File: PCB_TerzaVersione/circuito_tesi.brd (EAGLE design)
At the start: 100 x 80 mm, 57 parts, among them IC1 SCD41-D-R2, J2 S5B-ZR-SM4A-TF_(LF)_(SN)CONN_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, Q1 BSS138, Q2 BSS138, Q3 BSS138, Q4 BSS138, U1 STMICROELECTRONICS_LIS3DHSTMI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, U3 MICS-6814, U6 BME280, Y1 ECS-.327-9-16-TR

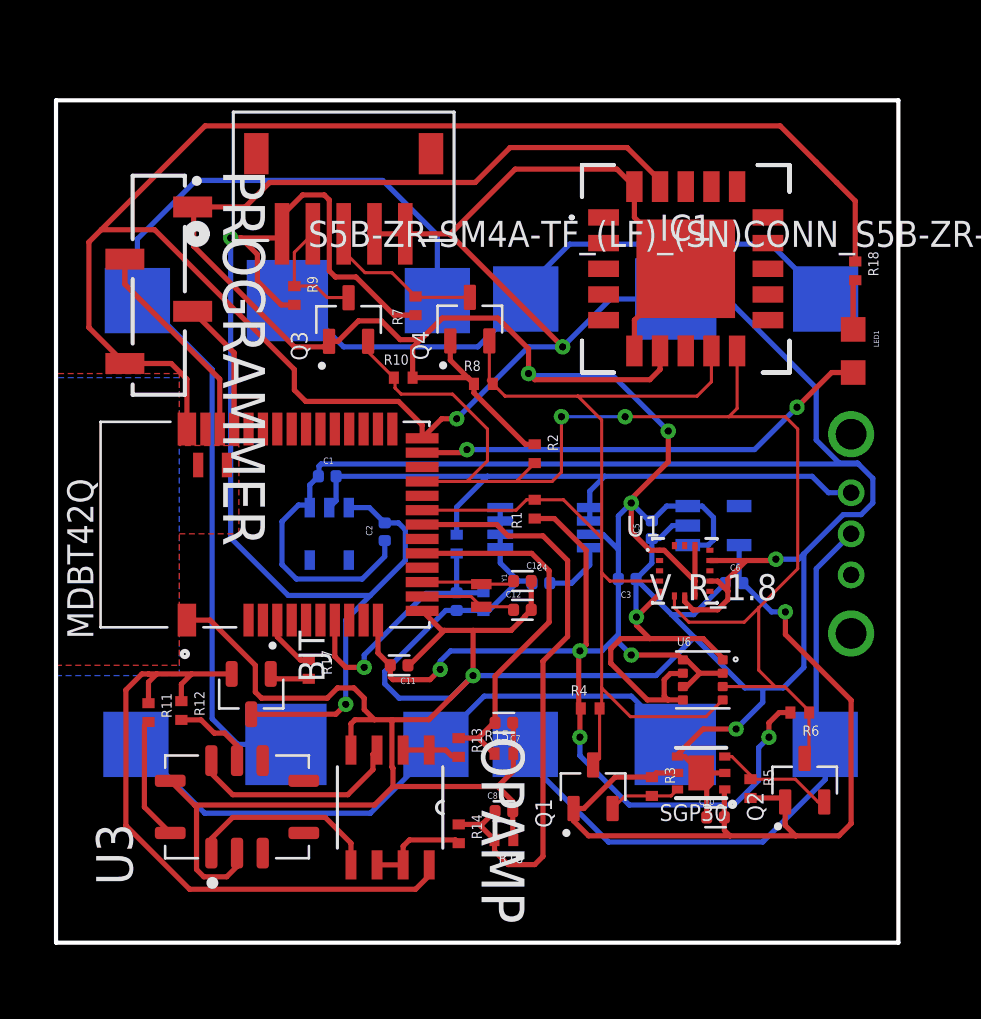
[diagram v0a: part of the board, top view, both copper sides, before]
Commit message: Cambiato collegamento BJT
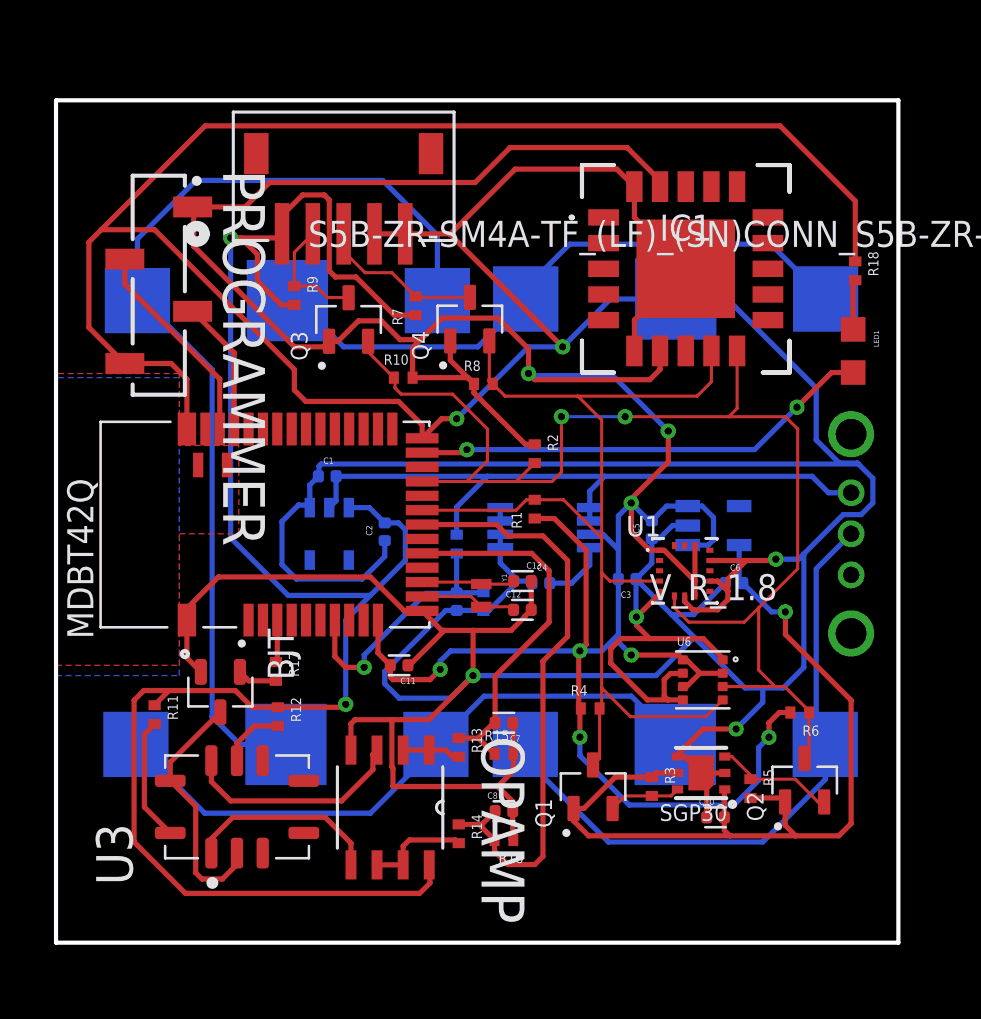
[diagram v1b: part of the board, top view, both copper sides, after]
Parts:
- moved R12 4.71 mm to (20.8, 38.0)
- moved R17 1.60 mm to (20.7, 40.2)
- moved BJT 1.50 mm to (18.0, 39.2)
- moved R11 0.32 mm to (14.8, 38.1)
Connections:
- net 5V: now also OPAMP.8, R11.1, R12.1; no longer BJT.3
- net BJT: now also BJT.3, U3.B, U3.J; no longer BJT.2, OPAMP.8, R11.1, R12.1
- net GND: now also BJT.2; no longer U3.B, U3.J
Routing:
- net 5V: track 59.8 -> 90.3 mm
- net BJT: track 32.0 -> 12.3 mm
- net GND: track 344.6 -> 330.3 mm
- net N$11: track 3.96 -> 3.19 mm
- net P8: track 2.81 -> 2.07 mm

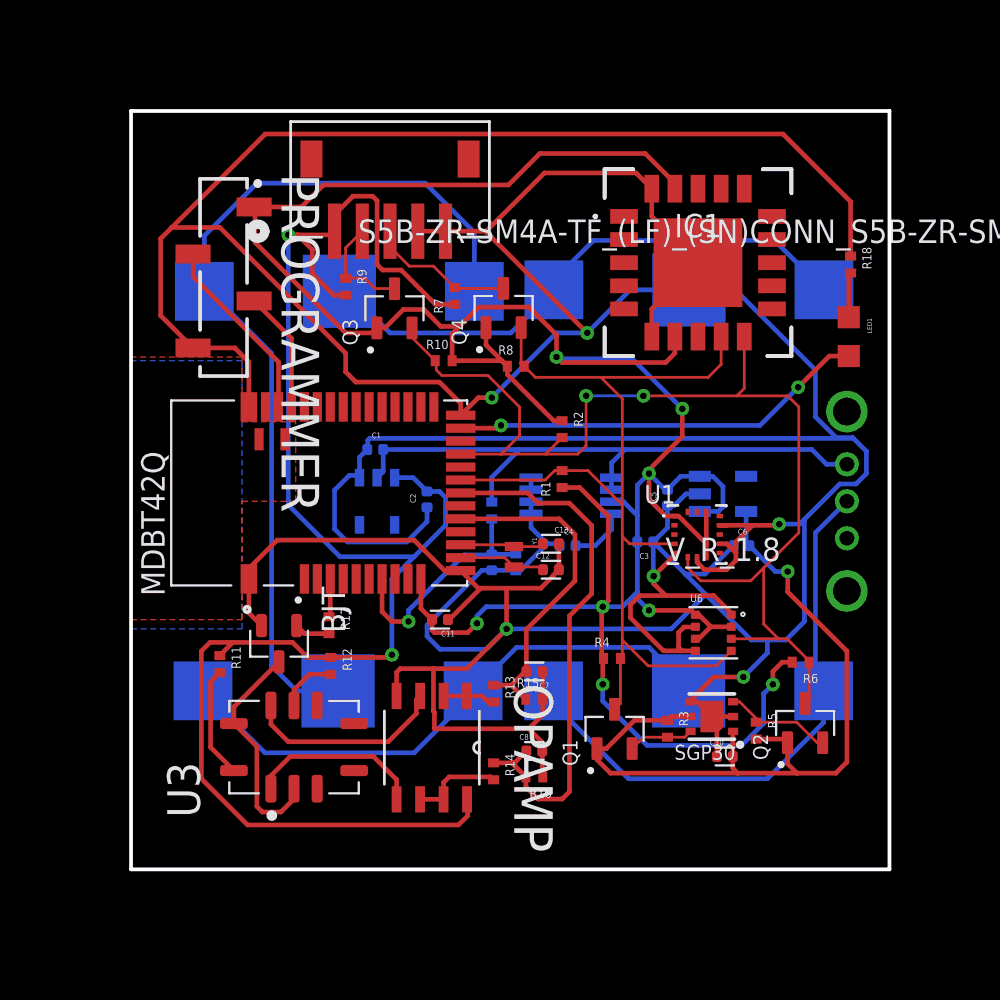
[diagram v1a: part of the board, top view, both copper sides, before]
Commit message: Resistenze con valore esatto
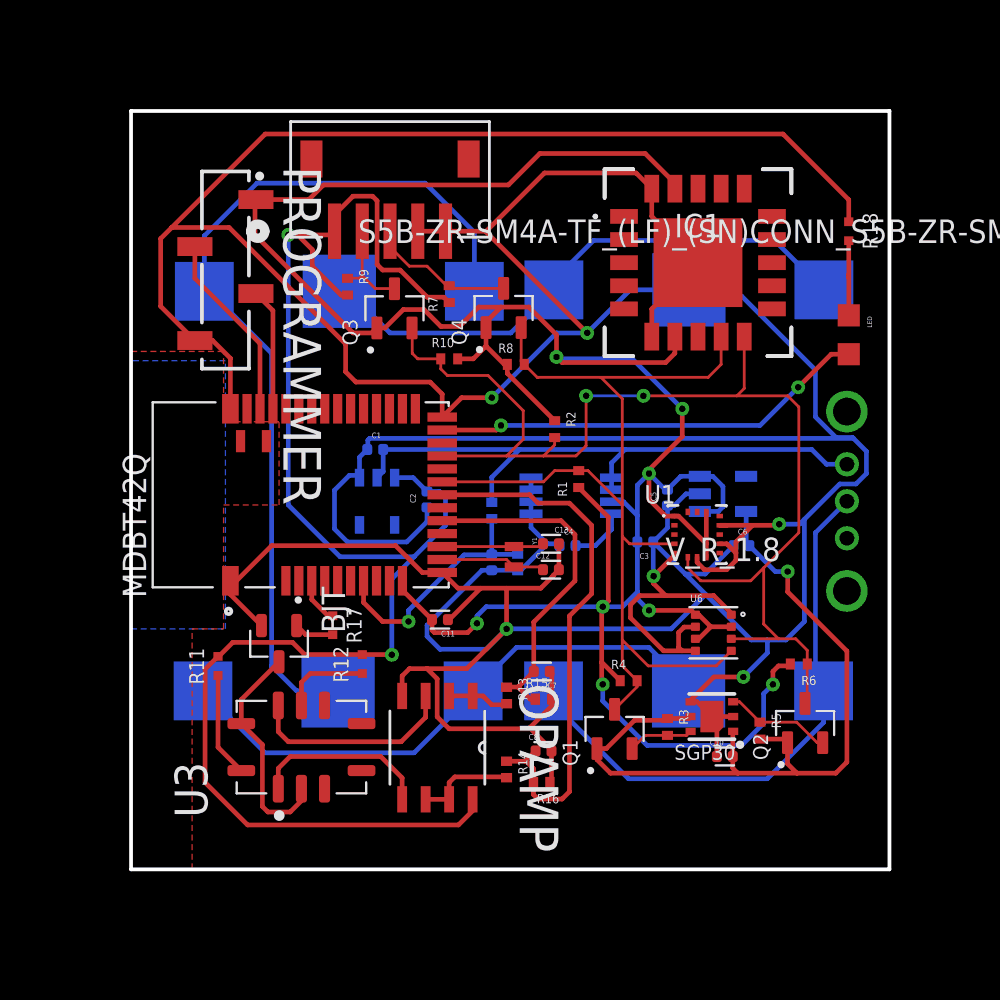
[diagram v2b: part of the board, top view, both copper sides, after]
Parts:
- removed LED1: LTST-C170TBKT, LED_0805:DIOC200X125X110
- added LED: LTST-C170KRKT, LED_R_LTST-C170KRKT:DIOC200X125X110
- R1, R10, R2, R3, R4, R5, R6, R7, R8, R9: value 8-1879333-9 -> MCS0402MC1002FE000; device Resistenza_case_0402:RESC1005X35N -> Res_10K_0402:RESC1005X37N
- R11: value 8-1879333-9 -> ERJPA2F1300X; device Resistenza_case_0402:RESC1005X35N -> Res_130_0402:RES_ERJPA2F1300X
- R12: value 8-1879333-9 -> ERJPA2J821X; device Resistenza_case_0402:RESC1005X35N -> Res_820_0402:RES_ERJPA2J821X
- R13, R14, R19, R20: value 8-1879333-9 -> ERJ-2GEJ515X; device Resistenza_case_0402:RESC1005X35N -> Res_5,1M_0402:RESC1005X40N
- R15, R16: value 8-1879333-9 -> ERJ-2GEJ106X; device Resistenza_case_0402:RESC1005X35N -> Res_10M_0402:RESC1005X40N
- R17: value 8-1879333-9 -> ERJPA2F5101X; device Resistenza_case_0402:RESC1005X35N -> Res_5,1K_0402:RES_ERJPA2F5101X
- R18: value 8-1879333-9 -> ERA2AEB331X; device Resistenza_case_0402:RESC1005X35N -> Res_330_0402:RES_ERA2AEB331X
- moved R18 1.80 mm to (48.8, 61.5)
- moved R12 1.70 mm to (22.5, 38.1), turned to 90 degrees
- moved R4 1.50 mm to (36.9, 37.2)
- moved MDBT42Q 1.00 mm to (19.2, 47.2)
- moved R1 0.90 mm to (34.2, 48.1)
- moved R13 0.71 mm to (30.3, 36.4)
- moved R14 0.71 mm to (30.3, 32.4)
- moved R16 0.50 mm to (32.2, 31.7)
- moved C8 0.50 mm to (32.3, 33.4)
- moved R15 0.50 mm to (32.3, 36.2)
- moved PROGRAMMER 0.41 mm to (15.1, 59.4)
- moved C7 0.40 mm to (32.2, 37.7)
- moved U3 0.40 mm to (19.2, 33.6)
- moved R2 0.40 mm to (32.9, 50.8)
- moved R10 0.32 mm to (27.2, 54.6)
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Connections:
- net 5V: now also R11.2, R12.2; no longer R11.1, R12.1
- net LED: now also LED.+; no longer LED1.+
- net N$11: now also R12.1; no longer R12.2
- net N$13: now also R11.1; no longer R11.2
- net N$9: now also LED.-; no longer LED1.-
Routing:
- net SDA: track 63.2 -> 65.6 mm
- net 5V: track 90.3 -> 88.0 mm
- net GND: track 330.3 -> 328.6 mm
- net SCL: track 53.1 -> 54.7 mm
- net 3.3V: track 154.3 -> 152.7 mm
- net N$9: track 2.43 -> 4.04 mm
- net N$11: track 3.19 -> 4.74 mm
- net LED: track 22.6 -> 23.7 mm
- net N$18: track 4.55 -> 5.51 mm
- net N$17: track 4.72 -> 5.68 mm
- net BATTERY: track 13.0 -> 13.7 mm
- net AIN1: track 18.2 -> 18.8 mm
- net N$13: track 6.17 -> 5.67 mm

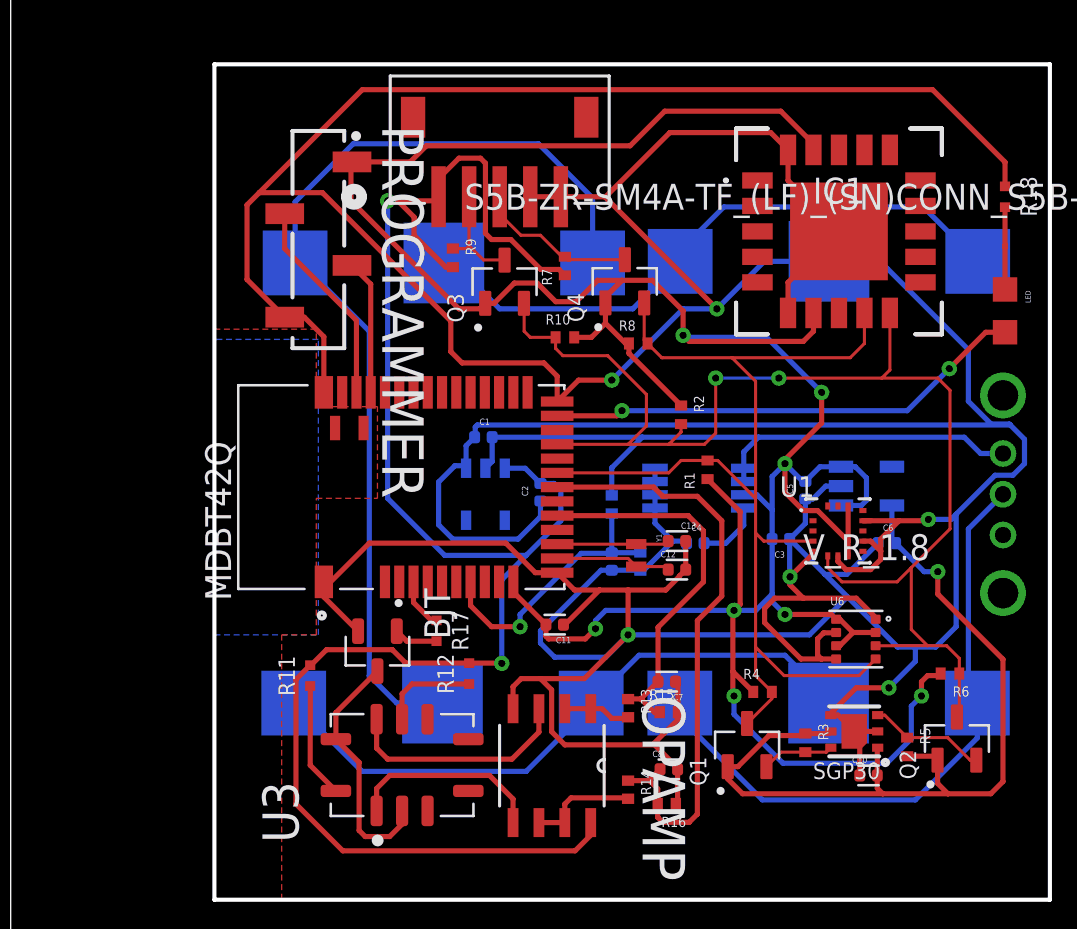
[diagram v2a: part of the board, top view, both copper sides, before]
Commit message: Messi condensatori corretti
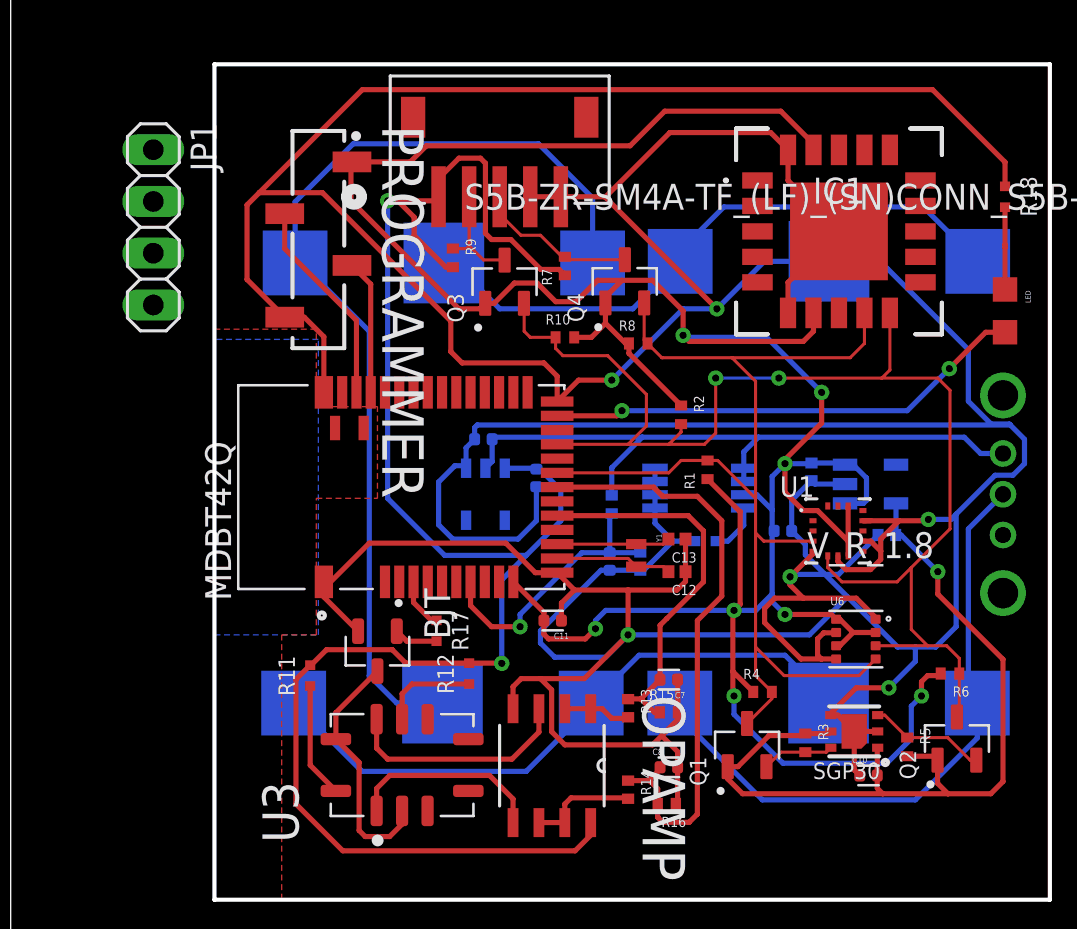
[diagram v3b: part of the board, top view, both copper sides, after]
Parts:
- added JP1: (no value), pinhead:1X04
- C1, C10, C2: value C0402H102J5GACTU -> C0402C104K9RACAUTO; device Condensatore_case_0402:CAPC1005X55N -> Cond_100n_0402:CAPC1005X55N
- C11: value C0402H102J5GACTU -> CL05A106MP5NUNC; device Condensatore_case_0402:CAPC1005X55N -> Cond_10u_0402:CAPC1005X55N
- C12, C13: value C0402H102J5GACTU -> 04025A120FAT2A; device Condensatore_case_0402:CAPC1005X55N -> Cond_12p_0402:CAPC1005X56N
- C3: value C0402H102J5GACTU -> CL05A225MQ5NNNC; device Condensatore_case_0402:CAPC1005X55N -> Cond_2,2u_0402:CAPC1005X55N
- C4: value C0402H102J5GACTU -> CL05B471KB5NNNCCAP_CL05_SAM; device Condensatore_case_0402:CAPC1005X55N -> Cond_470p_0402:CAP_CL05_SAM
- C5, C6: value C0402H102J5GACTU -> JMK105BJ105KV-F; device Condensatore_case_0402:CAPC1005X55N -> Cond_1u_0402:CAPC1005X55N
- C7, C8, C9: value C0402H102J5GACTU -> CL05B103KO5NNNC; device Condensatore_case_0402:CAPC1005X55N -> Cond_10n_0402:CAPC1005X55N
- moved C5 0.95 mm to (39.3, 48.0), turned to 90 degrees
- moved C2 0.73 mm to (25.8, 47.7)
- moved C4 0.51 mm to (34.1, 44.6), turned to 180 degrees
- moved C3 0.41 mm to (37.9, 45.1)
- moved C6 0.40 mm to (43.0, 44.9), turned to 180 degrees
- moved V_R_1.8 0.22 mm to (42.2, 47.4)
- moved C11 0.22 mm to (26.6, 40.7)
- moved C7 0.14 mm to (32.3, 37.8)
- moved C1 0.10 mm to (23.2, 49.6)
- moved C12 0.10 mm to (32.7, 43.1), turned to 180 degrees
- moved C13 0.10 mm to (32.7, 44.7), turned to 180 degrees
- moved C8 0.10 mm to (32.3, 33.5)
- moved C9 0.10 mm to (29.4, 43.6)
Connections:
- net 1.8V: now also C6.2; no longer C6.1
- net 3.3V: now also C5.2; no longer C5.1
- net GND: now also C12.1, C13.1, C4.1, C5.1, C6.1; no longer C12.2, C13.2, C4.2, C5.2, C6.2
- net N$14: now also C4.2; no longer C4.1
- net N$17: now also C12.2; no longer C12.1
- net N$18: now also C13.2; no longer C13.1
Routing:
- net GND: track 328.6 -> 330.6 mm
- net N$14: track 3.19 -> 2.53 mm

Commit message: Sistemati dei dettagli
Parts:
- removed JP1: (no value), pinhead:1X04
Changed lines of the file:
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@@
 <attribute name="VALUE" x="30.27" y="42.65" size="0.5" layer="28" rot="MR90" align="top-left"/>
-</element>
-<element name="JP1" library="pinhead" library_urn="urn:adsk.eagle:library:325" package="1X04" package3d_urn="urn:adsk.eagle:package:22407/2" value="" x="7" y="60" smashed="yes" rot="R270">
-<attribute name="NAME" x="8.8288" y="65.1562" size="1.27" layer="25" ratio="10" rot="R270"/>
-<attribute name="POPULARITY" value="91" x="7" y="60" size="1.778" layer="27" rot="R270" display="off"/>
-<attribute name="VALUE" x="3.825" y="65.08" size="1.27" layer="27" rot="R270"/>
 </element>
 <element name="C1" library="Cond_100n_0402" package="CAPC1005X55N" value="C0402C104K9RACAUTO" x="23.2" y="49.6" smashed="yes" rot="MR0">
@@
 </board>
 </drawing>
-<compatibility>
-<note version="8.2" severity="warning">
-Since Version 8.2, EAGLE supports online libraries. The ids
-of those online libraries will not be understood (or retained)
-with this version.
-</note>
-<note version="8.3" severity="warning">
-Since Version 8.3, EAGLE supports URNs for individual library
-assets (packages, symbols, and devices). The URNs of those assets
-will not be understood (or retained) with this version.
-</note>
-<note version="8.3" severity="warning">
-Since Version 8.3, EAGLE supports the association of 3D packages
-with devices in libraries, schematics, and board files. Those 3D
-packages will not be understood (or retained) with this version.
-</note>
-</compatibility>
 </eagle>
